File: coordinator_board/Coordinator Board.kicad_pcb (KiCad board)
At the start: 4 copper layers, 45.5 x 39.6 mm, 30 parts, among them J1 Conn_01x04, J2 Conn_01x04, J3 Conn_01x04, P4 SERIAL, SW1 Switch_SPDT_x2, SW2 Switch_DPST, U0 10118194, U1 LM3671, U2 CD74HC4050, U3 ESP-12E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

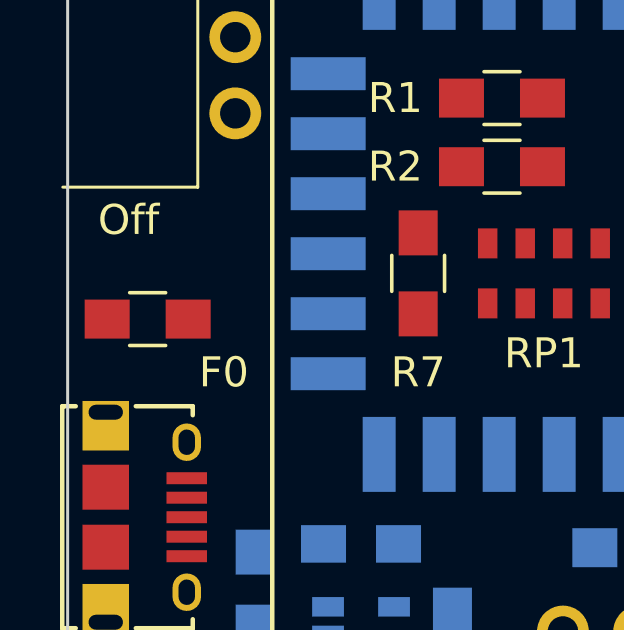
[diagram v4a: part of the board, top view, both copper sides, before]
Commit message: Added power planes and small tweaks
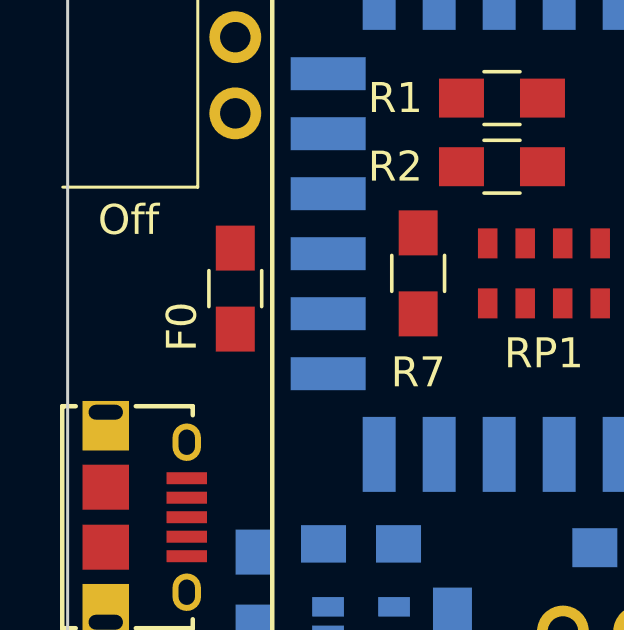
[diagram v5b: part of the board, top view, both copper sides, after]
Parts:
- moved F0 3.09 mm to (99.5, 116.6), turned to 270 degrees
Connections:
- U6 pad 6: +5V -> +3V3
- U7 pad 6: +5V -> +3V3
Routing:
- added copper zone on Power.Plane, net +3V3
- added copper zone on Power.Plane, net +5V
- added copper zone on Ground.Plane, net GND
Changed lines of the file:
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@@
   (general
     (links 93)
-    (no_connects 93)
-    (area 83.099791 94.941314 150.475639 150.023401)
+    (no_connects 82)
+    (area 93.869999 103.109999 139.436001 142.834001)
     (thickness 1.6)
     (drawings 7)
@@
   (layers
     (0 F.Cu signal)
-    (1 Ground.Plane power)
-    (2 Power.Plane power)
+    (1 Ground.Plane power hide)
+    (2 Power.Plane power hide)
     (31 B.Cu signal)
     (32 B.Adhes user)
@@
       (net 29 "Net-(U3-Pad21)"))
     (pad 6 smd rect (at 1.35 -0.95 90) (size 1.56 0.65) (layers F.Cu F.Paste F.Mask)
-      (net 15 +5V))
+      (net 5 +3V3))
     (pad 5 smd rect (at 1.35 0 90) (size 1.56 0.65) (layers F.Cu F.Paste F.Mask)
       (net 4 GND))
@@
       (net 30 "Net-(U3-Pad22)"))
     (pad 6 smd rect (at 1.35 -0.95 90) (size 1.56 0.65) (layers F.Cu F.Paste F.Mask)
-      (net 15 +5V))
+      (net 5 +3V3))
     (pad 5 smd rect (at 1.35 0 90) (size 1.56 0.65) (layers F.Cu F.Paste F.Mask)
       (net 4 GND))
@@
   )
   (module Resistors_SMD:R_0805_HandSoldering (layer F.Cu)
-    (at 96.587 117.638)
+    (at 99.508 116.622 270)
     (descr "Resistor SMD 0805, hand soldering")
     (tags "resistor 0805")
     (attr smd)
-    (fp_text reference F0 (at 2.54 1.778) (layer F.SilkS)
-      (effects (font (size 1 1) (thickness 0.15)))
-    )
-    (fp_text value Fuse (at 0 1.75) (layer F.Fab) hide
-      (effects (font (size 1 1) (thickness 0.15)))
-    )
-    (fp_text user %R (at 0 0) (layer F.Fab)
+    (fp_text reference F0 (at 1.27 1.778 270) (layer F.SilkS)
+      (effects (font (size 1 1) (thickness 0.15)))
+    )
+    (fp_text value Fuse (at 0 1.75 270) (layer F.Fab) hide
+      (effects (font (size 1 1) (thickness 0.15)))
+    )
+    (fp_text user %R (at 0 0 270) (layer F.Fab)
       (effects (font (size 0.5 0.5) (thickness 0.075)))
     )
@@
     (fp_line (start 2.35 0.9) (end 2.35 -0.9) (layer F.CrtYd) (width 0.05))
     (fp_line (start 2.35 0.9) (end -2.35 0.9) (layer F.CrtYd) (width 0.05))
-    (pad 1 smd rect (at -1.35 0) (size 1.5 1.3) (layers F.Cu F.Paste F.Mask)
+    (pad 1 smd rect (at -1.35 0 270) (size 1.5 1.3) (layers F.Cu F.Paste F.Mask)
       (net 31 "Net-(F0-Pad1)"))
-    (pad 2 smd rect (at 1.35 0) (size 1.5 1.3) (layers F.Cu F.Paste F.Mask)
+    (pad 2 smd rect (at 1.35 0 270) (size 1.5 1.3) (layers F.Cu F.Paste F.Mask)
       (net 32 "Net-(F0-Pad2)"))
     (model ${KISYS3DMOD}/Resistors_SMD.3dshapes/R_0805.wrl
@@
     (effects (font (size 1 1) (thickness 0.15)))
   )
+  (zone (net 4) (net_name GND) (layer Ground.Plane) (hatch edge 0.508)
+    (connect_pads (clearance 0.508))
+    (min_thickness 0.254)
+    (fill yes (arc_segments 16) (thermal_gap 0.508) (thermal_bridge_width 0.508))
+    (polygon
+      (pts
+        (xy 119.32 123.988) (xy 139.386 123.988) (xy 139.386 142.784) (xy 93.92 142.784) (xy 93.92 103.16)
+        (xy 119.32 103.16)
+      )
+    )
+  )
+  (zone (net 15) (net_name +5V) (layer Power.Plane) (hatch edge 0.508)
+    (connect_pads (clearance 0.508))
+    (min_thickness 0.254)
+    (fill yes (arc_segments 16) (thermal_gap 0.508) (thermal_bridge_width 0.508))
+    (polygon
+      (pts
+        (xy 102.556 114.336) (xy 102.81 129.322) (xy 139.386 129.322) (xy 139.386 142.784) (xy 93.92 142.784)
+        (xy 93.92 103.16) (xy 102.556 103.16)
+      )
+    )
+  )
+  (zone (net 5) (net_name +3V3) (layer Power.Plane) (hatch edge 0.508)
+    (connect_pads (clearance 0.508))
+    (min_thickness 0.254)
+    (fill yes (arc_segments 16) (thermal_gap 0.508) (thermal_bridge_width 0.508))
+    (polygon
+      (pts
+        (xy 119.828 124.242) (xy 127.702 124.242) (xy 127.702 120.94) (xy 139.386 120.94) (xy 139.386 128.56)
+        (xy 103.572 128.56) (xy 103.318 103.414) (xy 120.082 103.414)
+      )
+    )
+  )
 )

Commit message: Finished first draft of the board
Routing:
- net GND: track 0.00 -> 63.9 mm, vias 0 -> 7
- net Net-(RP1-Pad1): track 0.00 -> 48.6 mm, vias 0 -> 3
- net Net-(R7-Pad2): track 0.00 -> 45.5 mm, vias 0 -> 2
- net Net-(U3-Pad22): track 0.00 -> 45.5 mm, vias 0 -> 1
- net Net-(RP1-Pad2): track 0.00 -> 44.7 mm, vias 0 -> 2
- net Net-(RP1-Pad3): track 0.00 -> 42.2 mm, vias 0 -> 2
- net Net-(D1-Pad2): track 0.00 -> 41.6 mm, vias 0 -> 1
- net Net-(U3-Pad21): track 0.00 -> 41.4 mm, vias 0 -> 1
- net Net-(R2-Pad1): track 0.00 -> 39.6 mm, vias 0 -> 2
- net Net-(RP1-Pad4): track 0.00 -> 37.5 mm, vias 0 -> 2
- net Net-(P4-Pad2): track 0.00 -> 35.7 mm, vias 0 -> 1
- net Net-(P4-Pad1): track 0.00 -> 34.3 mm, vias 0 -> 1
- net +3V3: track 0.00 -> 29.4 mm, vias 0 -> 5
- net Net-(J1-Pad2): track 0.00 -> 23.8 mm, vias 0 -> 1
- net +5V: track 0.00 -> 21.9 mm, vias 0 -> 4
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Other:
- rule pad_to_mask_clearance: 0 -> 0.0508
